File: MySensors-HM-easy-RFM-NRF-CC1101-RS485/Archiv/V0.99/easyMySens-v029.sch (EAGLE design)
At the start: 52 parts, among them IC1 ATSHA204A, IC2 REG1117, M1 ARDUINO-PRO-MINI-3.3V#NP, M2 NRF24L01+SMD, X1 1751280, X3 1751280

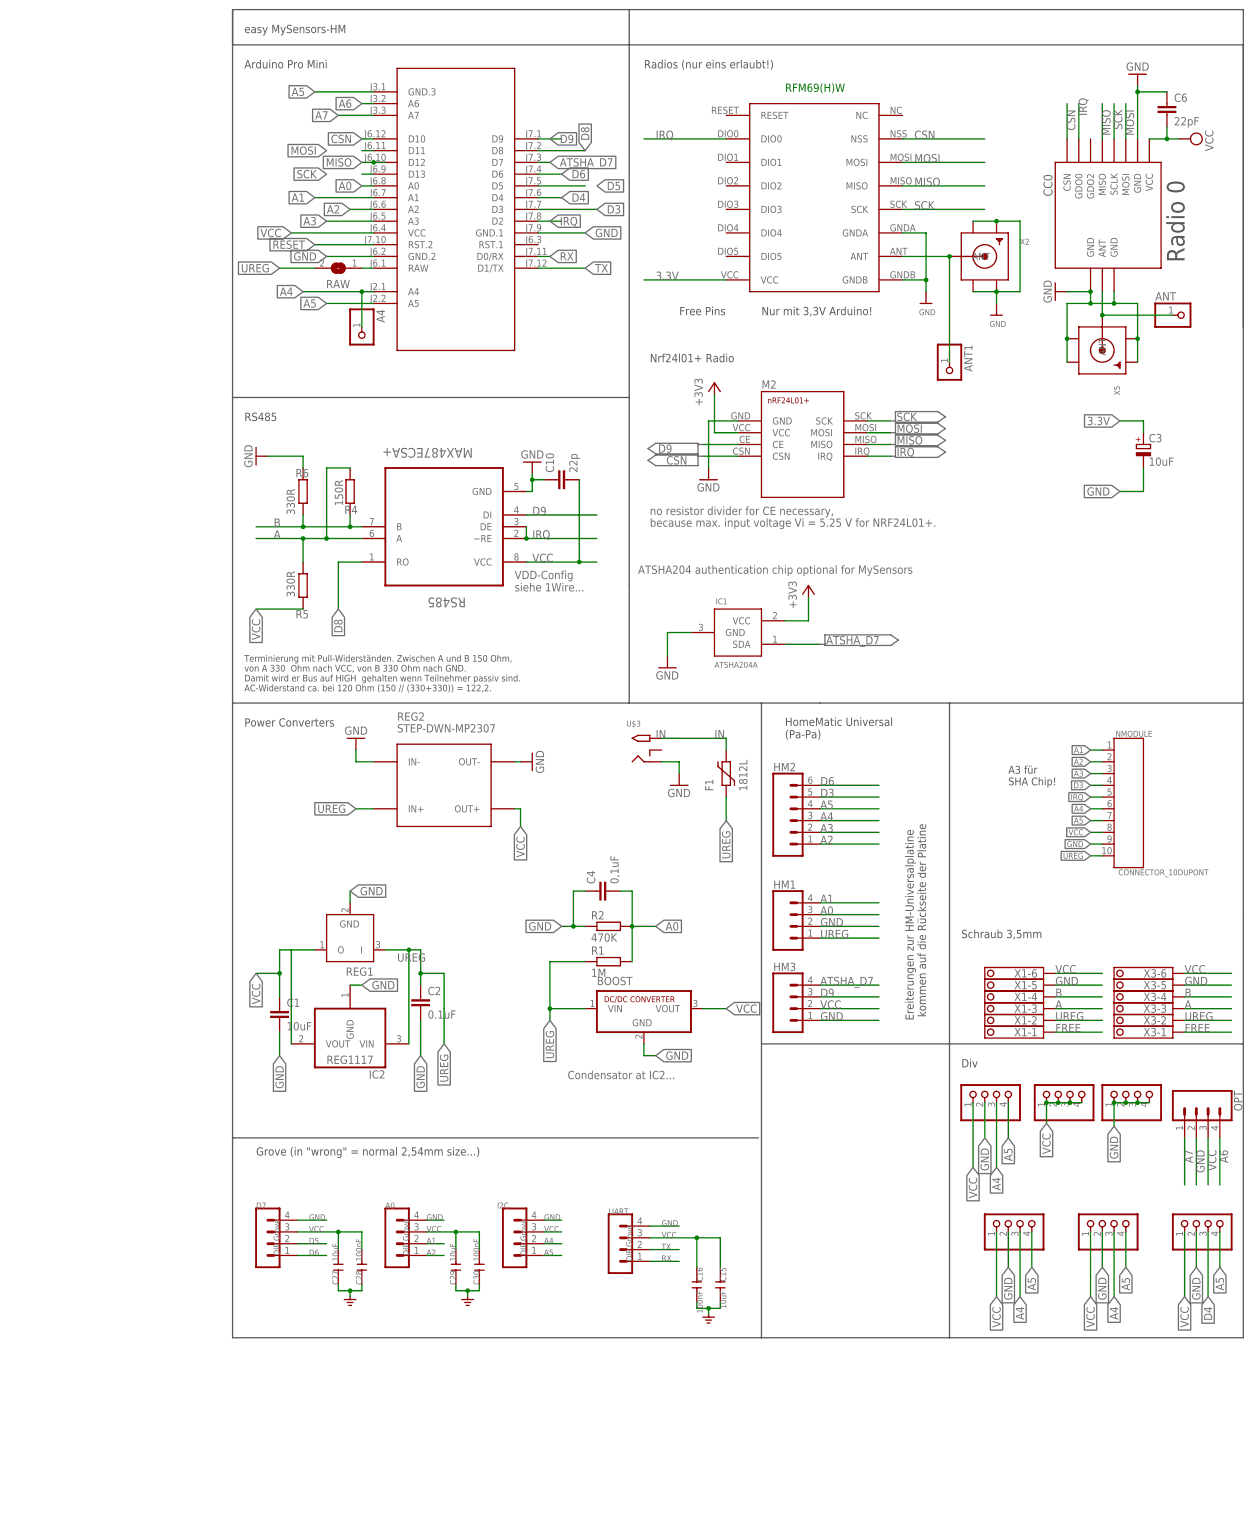
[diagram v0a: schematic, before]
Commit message: Some new easyBoards
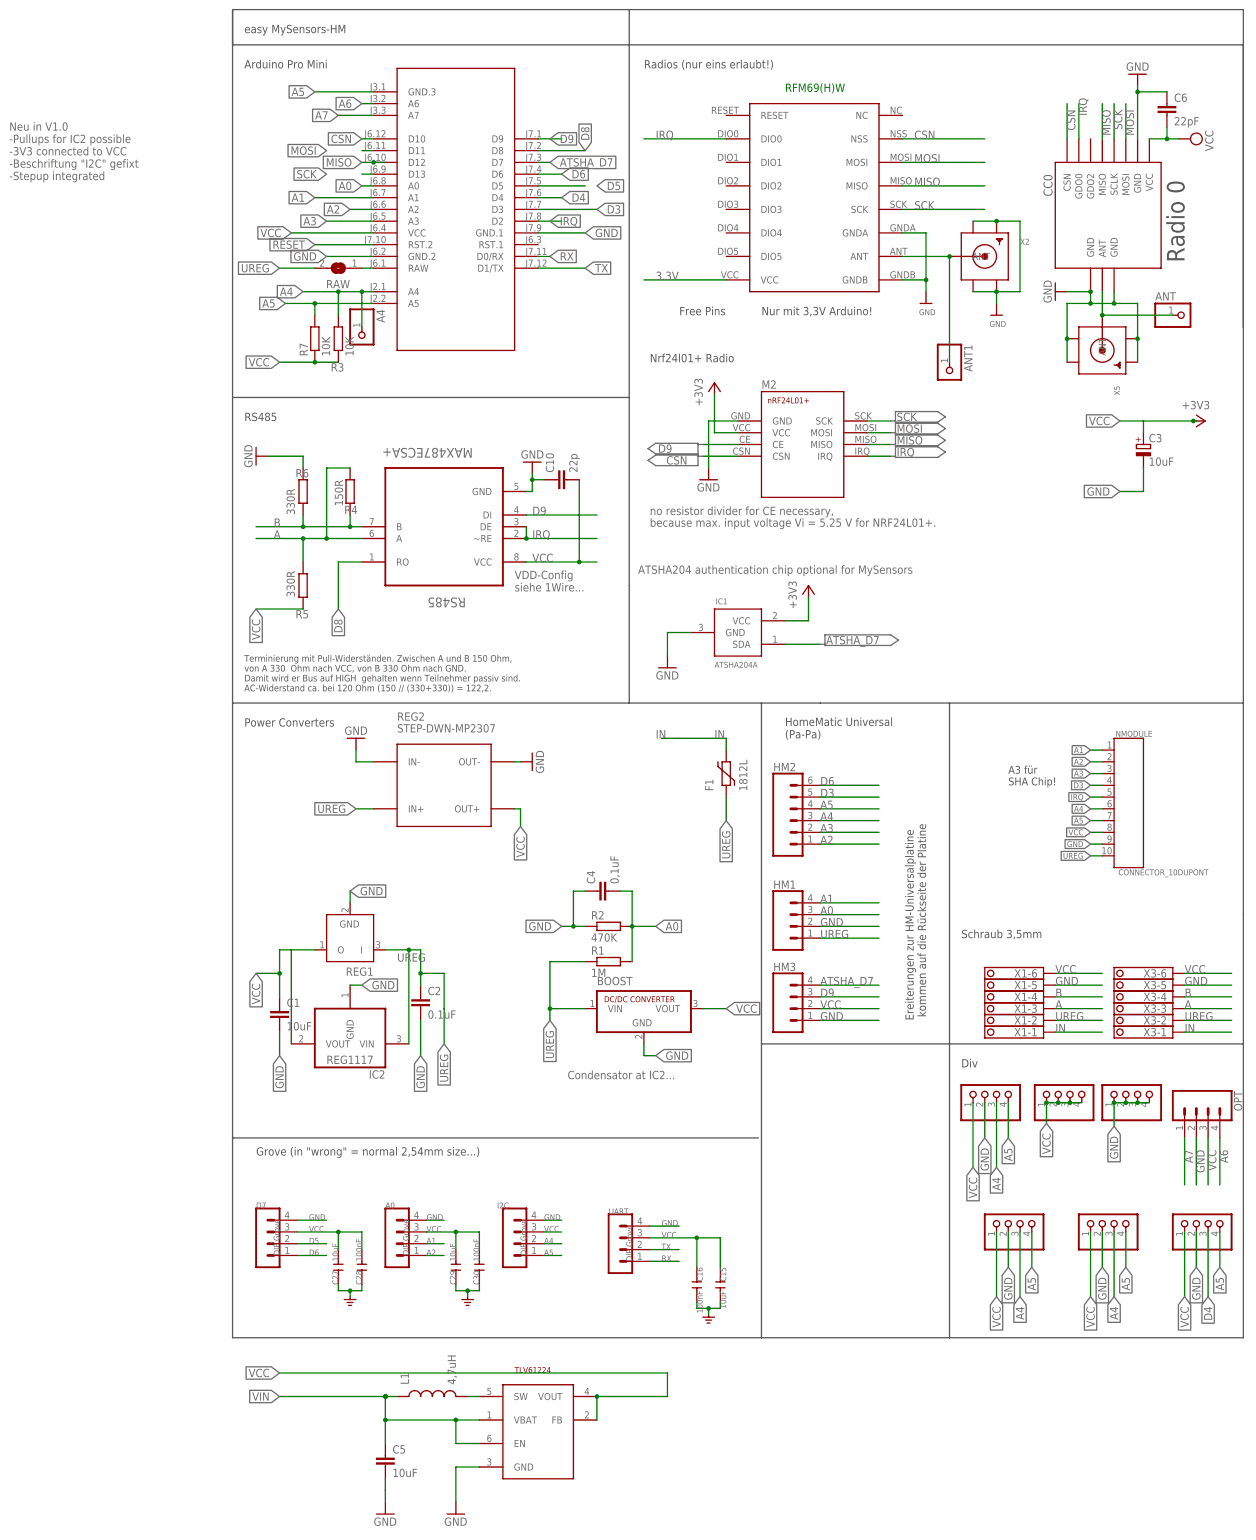
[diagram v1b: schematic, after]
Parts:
- removed U$3: 2.1MMJACKTHM, adafruit:2.1MMJACKTHM
- added C5: 10uF, SparkFun-Passives:CAP0805
- added L1: 4,7uH, SparkFun-Passives:INDUCTOR0805
- added R3, R7: 10K, rcl:R-EU_R0805
- added STEPUP: TLV61224, TLV61224:TI-TLV61224
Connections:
- removed net FREE: X1-1.K, X3-1.K
- new net N$13: L1.2, STEPUP.SW
- new net VIN: C5.1, L1.1, STEPUP.EN, STEPUP.VBAT
- net 3.3V: no longer C3.+
- net A4: now also R3.2
- net A5: now also R7.2
- net GND: now also C5.2, STEPUP.GND; no longer U$3.RING
- net IN: now also X1-1.K, X3-1.K; no longer U$3.TIP
- net VCC: now also C3.+, R3.1, R7.1, STEPUP.FB, STEPUP.VOUT
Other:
- note added: "Neu in V1.0 -Pullups for IC2 possible -3V3 connected to VCC -Beschriftung "I2C" gefixt -Stepup integrated"
